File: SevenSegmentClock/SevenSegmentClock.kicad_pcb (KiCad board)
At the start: 2 copper layers, 337 x 76.1 mm, 125 parts, among them J1 12V, J2 GND, Q1 PN2222A, Q2 PN2222A, Q3 PN2222A, Q4 PN2222A, Q5 PN2222A, Q6 PN2222A, Q7 13N50F, U1 4511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

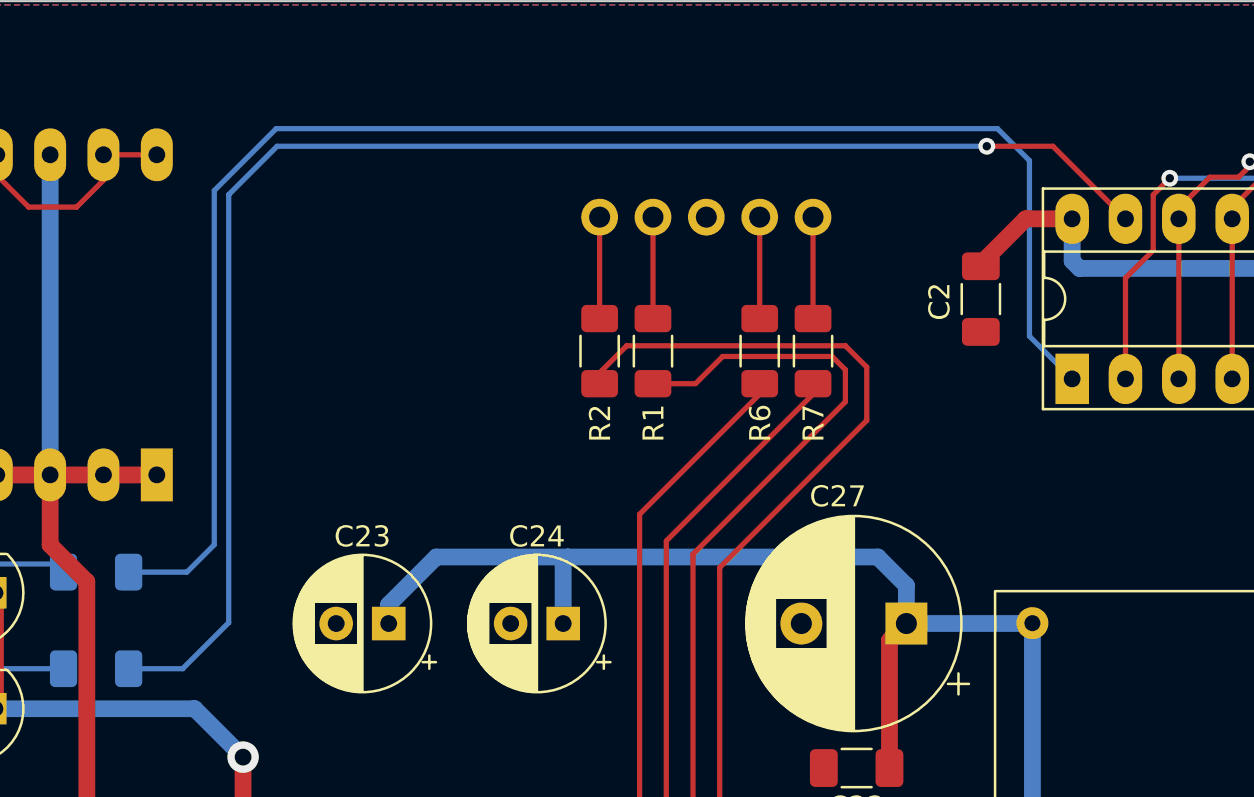
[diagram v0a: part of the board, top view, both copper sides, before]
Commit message: Swapping around percentage and degree indicators
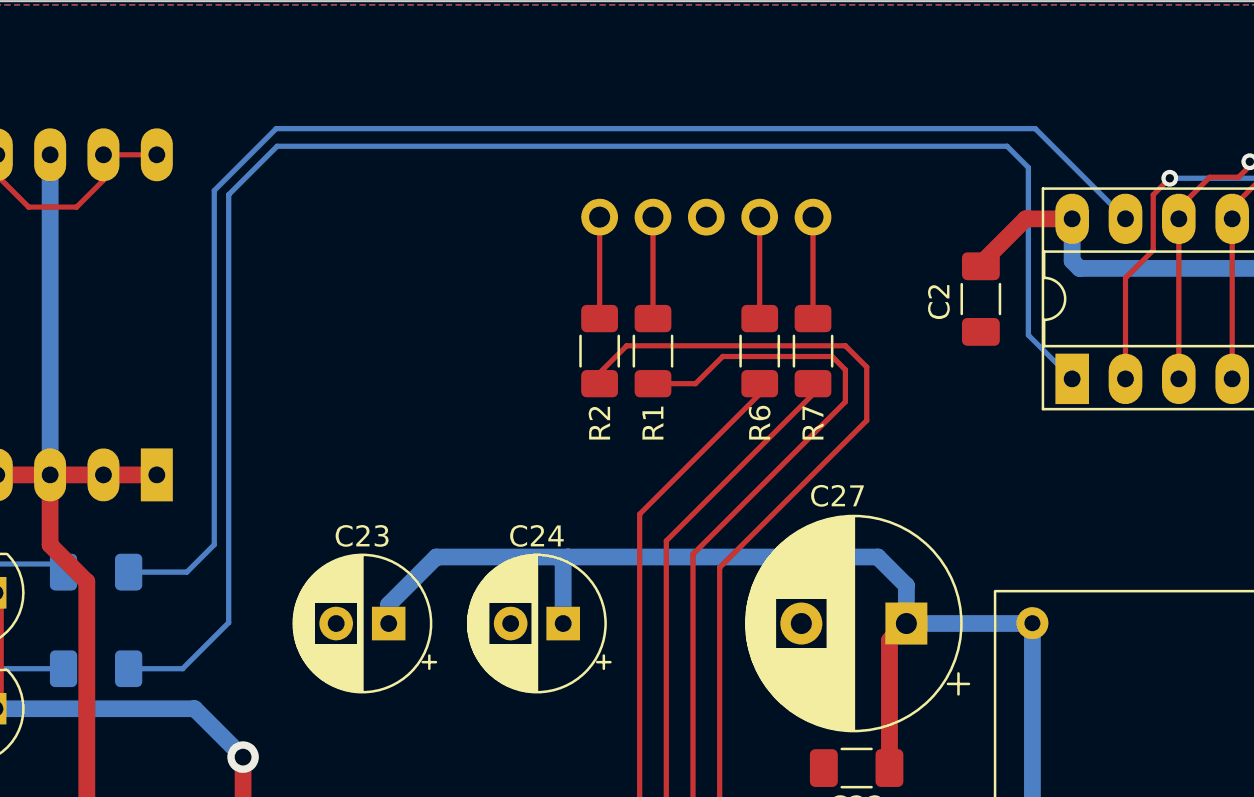
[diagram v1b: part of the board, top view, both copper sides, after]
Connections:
- U9 pad 1: /Display/DispDegree -> /Display/DispPercent
- U9 pad 13: /Display/DispPercent -> /Display/DispDegree
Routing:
- net /Display/DispDegree: track 73.4 -> 67.9 mm
- net /Display/DispPercent: track 71.1 -> 76.4 mm, vias 1 -> 0

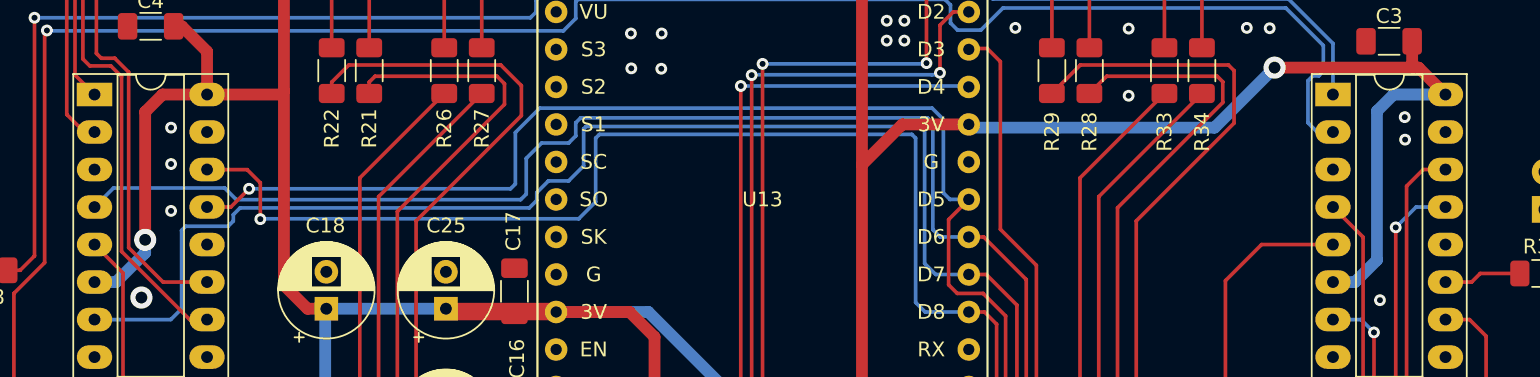
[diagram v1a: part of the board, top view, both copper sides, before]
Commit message: Fixing the polarity of the CD4042s
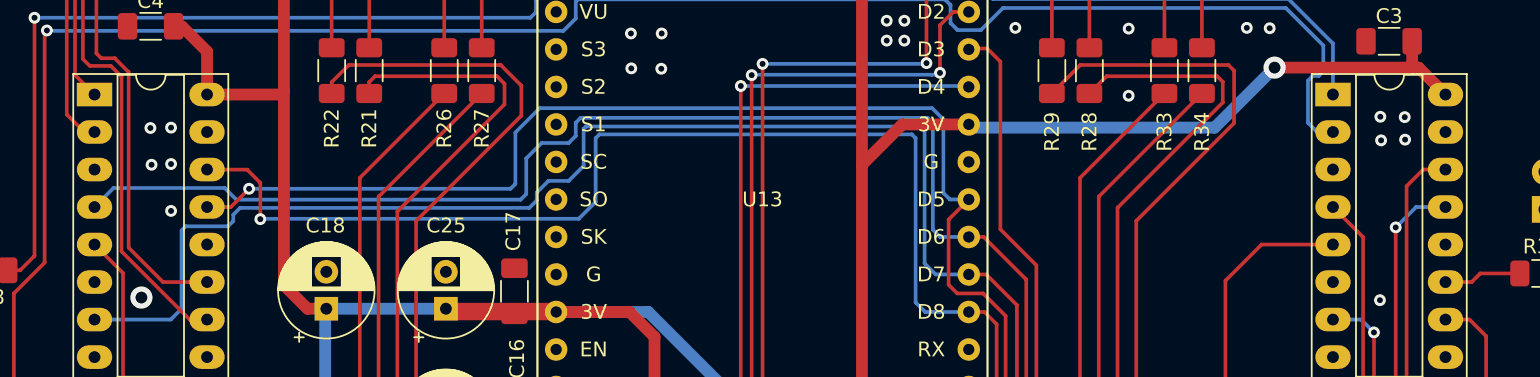
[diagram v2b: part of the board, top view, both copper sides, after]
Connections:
- U10 pad 6: +3.3V -> GND
- U4 pad 6: +3.3V -> GND
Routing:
- net +3.3V: track 469.7 -> 432.4 mm, vias 4 -> 3
- net GND: vias 37 -> 41
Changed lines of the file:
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@@
       (net 144 "Net-(U10-Clk)") (pinfunction "Clk") (pintype "input"))
     (pad "6" thru_hole oval (at 0 12.7) (size 2.4 1.6) (drill 0.8) (layers "*.Cu" "*.Mask")
-      (net 98 "+3.3V") (pinfunction "Pol") (pintype "input"))
+      (net 1 "GND") (pinfunction "Pol") (pintype "input"))
     (pad "7" thru_hole oval (at 0 15.24) (size 2.4 1.6) (drill 0.8) (layers "*.Cu" "*.Mask")
       (net 56 "DispB") (pintype "input"))
@@
       (net 62 "/Display/DotsClk") (pinfunction "Clk") (pintype "input"))
     (pad "6" thru_hole oval (at 0 12.7) (size 2.4 1.6) (drill 0.8) (layers "*.Cu" "*.Mask")
-      (net 98 "+3.3V") (pinfunction "Pol") (pintype "input"))
+      (net 1 "GND") (pinfunction "Pol") (pintype "input"))
     (pad "7" thru_hole oval (at 0 15.24) (size 2.4 1.6) (drill 0.8) (layers "*.Cu" "*.Mask")
       (net 56 "DispB") (pintype "input"))
@@
     (effects (font (size 1 1) (thickness 0.15)))
   )
+  (via (at 189.0522 98.425) (size 0.8) (drill 0.4) (layers "F.Cu" "B.Cu") (free) (net 1))
   (via (at 240.03 90.0176) (size 0.8) (drill 0.4) (layers "F.Cu" "B.Cu") (free) (net 1))
   (via (at 264.7696 89.1794) (size 0.8) (drill 0.4) (layers "F.Cu" "B.Cu") (free) (net 1))
@@
   (via (at 240.03 88.6714) (size 0.8) (drill 0.4) (layers "F.Cu" "B.Cu") (free) (net 1))
   (via (at 272.2372 107.5944) (size 0.8) (drill 0.4) (layers "F.Cu" "B.Cu") (free) (net 1))
+  (via (at 272.3134 96.774) (size 0.8) (drill 0.4) (layers "F.Cu" "B.Cu") (free) (net 1))
   (via (at 183.134 127.9144) (size 0.8) (drill 0.4) (layers "F.Cu" "B.Cu") (free) (net 1))
   (via (at 196.5706 129.413) (size 0.8) (drill 0.4) (layers "F.Cu" "B.Cu") (free) (net 1))
@@
   (via (at 277.0632 115.9256) (size 0.8) (drill 0.4) (layers "F.Cu" "B.Cu") (free) (net 1))
   (via (at 223.5962 89.535) (size 0.8) (drill 0.4) (layers "F.Cu" "B.Cu") (free) (net 1))
+  (via (at 188.976 95.9358) (size 0.8) (drill 0.4) (layers "F.Cu" "B.Cu") (free) (net 1))
   (via (at 223.5708 91.9226) (size 0.8) (drill 0.4) (layers "F.Cu" "B.Cu") (free) (net 1))
   (via (at 190.373 95.9104) (size 0.8) (drill 0.4) (layers "F.Cu" "B.Cu") (free) (net 1))
   (via (at 221.5134 89.535) (size 0.8) (drill 0.4) (layers "F.Cu" "B.Cu") (free) (net 1))
+  (via (at 272.2626 95.1738) (size 0.8) (drill 0.4) (layers "F.Cu" "B.Cu") (free) (net 1))
   (via (at 277.0886 117.4242) (size 0.8) (drill 0.4) (layers "F.Cu" "B.Cu") (free) (net 1))
   (via (at 255.2192 89.2048) (size 0.8) (drill 0.4) (layers "F.Cu" "B.Cu") (free) (net 1))
@@
   (segment (start 116.1274 85.7518) (end 118.3378 85.7518) (width 0.8) (layer "F.Cu") (net 98))
   (segment (start 224.4007 146.7021) (end 225.3996 147.701) (width 0.8) (layer "F.Cu") (net 98))
-  (segment (start 189.7966 93.6674) (end 192.8104 93.6674) (width 0.8) (layer "F.Cu") (net 98))
   (segment (start 185.1746 129.7296) (end 185.1746 129.2012) (width 0.8) (layer "F.Cu") (net 98))
   (segment (start 221.4236 108.3936) (end 223.1136 110.0836) (width 0.8) (layer "F.Cu") (net 98))
@@
   (segment (start 250.1574 82.9714) (end 252.3344 82.9714) (width 0.8) (layer "F.Cu") (net 98))
   (segment (start 248.5898 80.5688) (end 250.1574 82.1364) (width 0.8) (layer "F.Cu") (net 98))
-  (segment (start 188.6204 94.8436) (end 189.7966 93.6674) (width 0.8) (layer "F.Cu") (net 98))
   (segment (start 213.628 108.55372) (end 216.29198 108.55372) (width 0.8) (layer "F.Cu") (net 98))
   (segment (start 190.5529 89.0496) (end 191.1068 89.0496) (width 0.8) (layer "F.Cu") (net 98))
@@
   (segment (start 213.628 108.55372) (end 209.36632 108.55372) (width 0.8) (layer "F.Cu") (net 98))
   (segment (start 191.1068 89.0496) (end 192.8104 90.7532) (width 0.8) (layer "F.Cu") (net 98))
-  (segment (start 188.6204 103.505) (end 188.6204 94.8436) (width 0.8) (layer "F.Cu") (net 98))
   (segment (start 237.1598 98.425) (end 239.8912 95.6936) (width 0.8) (layer "F.Cu") (net 98))
   (segment (start 198.0184 106.5784) (end 199.6136 108.1736) (width 0.8) (layer "F.Cu") (net 98))
@@
   (segment (start 263.7028 128.2192) (end 265.1237 129.6401) (width 0.8) (layer "F.Cu") (net 98))
   (segment (start 266.2682 129.2352) (end 267.4508 128.0526) (width 0.8) (layer "F.Cu") (net 98))
-  (via (at 188.6204 103.505) (size 1.5) (drill 0.8) (layers "F.Cu" "B.Cu") (net 98))
   (via (at 263.7028 118.5672) (size 1.5) (drill 0.8) (layers "F.Cu" "B.Cu") (net 98))
   (via (at 265.0998 91.8464) (size 1.5) (drill 0.8) (layers "F.Cu" "B.Cu") (net 98))
@@
   (segment (start 263.7028 118.5672) (end 263.6892 118.5536) (width 0.8) (layer "B.Cu") (net 98))
   (segment (start 131.2164 88.1126) (end 118.6942 88.1126) (width 0.8) (layer "B.Cu") (net 98))
-  (segment (start 270.5432 106.3674) (end 272.034 104.8766) (width 0.8) (layer "B.Cu") (net 98))
-  (segment (start 272.034 104.8766) (end 272.034 94.7928) (width 0.8) (layer "B.Cu") (net 98))
   (segment (start 191.897 86.6902) (end 190.5508 86.6902) (width 0.8) (layer "B.Cu") (net 98))
   (segment (start 190.5508 86.6902) (end 157.5308 86.6902) (width 0.8) (layer "B.Cu") (net 98))
@@
   (segment (start 232.8536 118.5536) (end 222.6936 108.3936) (width 0.8) (layer "B.Cu") (net 98))
   (segment (start 156.1084 88.1126) (end 131.2164 88.1126) (width 0.8) (layer "B.Cu") (net 98))
-  (segment (start 269.0542 106.3674) (end 270.5432 106.3674) (width 0.8) (layer "B.Cu") (net 98))
   (segment (start 194.988 83.5992) (end 191.897 86.6902) (width 0.8) (layer "B.Cu") (net 98))
   (segment (start 200.8886 108.1736) (end 200.8124 108.2498) (width 0.8) (layer "B.Cu") (net 98))
@@
   (segment (start 222.6936 108.3936) (end 216.4521 108.3936) (width 0.8) (layer "B.Cu") (net 98))
   (segment (start 263.6892 118.5536) (end 244.3921 118.5536) (width 0.8) (layer "B.Cu") (net 98))
-  (segment (start 188.6204 104.394) (end 186.647 106.3674) (width 0.8) (layer "B.Cu") (net 98))
   (segment (start 118.3378 87.7562) (end 118.3378 85.7518) (width 0.8) (layer "B.Cu") (net 98))
   (segment (start 261.0358 95.9104) (end 265.0998 91.8464) (width 0.8) (layer "B.Cu") (net 98))
-  (segment (start 272.034 94.7928) (end 273.1594 93.6674) (width 0.8) (layer "B.Cu") (net 98))
-  (segment (start 188.6204 103.505) (end 188.6204 104.394) (width 0.8) (layer "B.Cu") (net 98))
   (segment (start 250.4186 95.9104) (end 244.6089 95.9104) (width 0.8) (layer "B.Cu") (net 98))
   (segment (start 194.988 82.0306) (end 194.988 83.5992) (width 0.8) (layer "B.Cu") (net 98))
   (segment (start 200.8124 115.9764) (end 199.517 117.2718) (width 0.8) (layer "B.Cu") (net 98))
-  (segment (start 186.647 106.3674) (end 185.1904 106.3674) (width 0.8) (layer "B.Cu") (net 98))
-  (segment (start 273.1594 93.6674) (end 276.6742 93.6674) (width 0.8) (layer "B.Cu") (net 98))
   (segment (start 250.4186 95.9104) (end 261.0358 95.9104) (width 0.8) (layer "B.Cu") (net 98))
   (segment (start 213.628 117.186479) (end 213.628 117.743) (width 0.8) (layer "F.Cu") (net 99))
